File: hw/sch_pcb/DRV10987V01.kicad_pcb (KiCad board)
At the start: 2 copper layers, 50.3 x 40.1 mm, 28 parts, among them IC1 DRV10987DPWPR, J10 3v3 or 5v, J11 WAGO, J12 WAGO, J2 HEADER_2x05_PARALLEL, J3 HEADER_2x04_PARALLEL, J4 HEADER_2x01, J5 AUX, J6 HEADER_2x03_PARALLEL, M1 HOLE M3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

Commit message: update silkscreen, add 5v indicator
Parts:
- added D2: LED, Mlab_D:LED_1206_2, F.Cu at (127.9, 95.9)
- added R6: R_Small, Resistor_SMD:R_0805_2012Metric, F.Cu at (128.6, 98.5)
- J10: value 3v3 or 5v -> PWR
- J2: value HEADER_2x05_PARALLEL -> I2C
- J4: value HEADER_2x01 -> JUMPER
- J6: value HEADER_2x03_PARALLEL -> MOTOR
- L1: value 47uH -> 47uH DE0703-47
- M3, M4: value HOLE -> HOLE M3
- R1, R2, R3, R4, R5: value 4k5 -> 4k7
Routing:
- net +5V: track 34.1 -> 42.1 mm
- net Net-(D2-A): track 0.00 -> 2.71 mm
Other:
- board text added: "5V"
- board text added: "5V output 100 mA"
- board text added: "DRV10987V01A mlab.cz, 2023"
- board text removed: "2023"
- board text removed: "5V/3V3 output 100 mA configurable"
- board text removed: "DRV10975V01A mlab.cz"

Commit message: Zmena strany sroubu
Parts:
- M1, M2, M3, M4: moved to B.Cu
- turned M1 to 180 degrees
- turned M2 to 180 degrees
- turned M3 to 180 degrees
- turned M4 to 180 degrees
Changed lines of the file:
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@@
-    )
-  )
-  (footprint "Mlab_Mechanical:MountingHole_3mm" placed (layer "F.Cu")
-    (at 168.82 89.76)
-    (descr "Mounting hole, Befestigungsbohrung, 3mm, No Annular, Kein Restring,")
-    (tags "Mounting hole, Befestigungsbohrung, 3mm, No Annular, Kein Restring,")
-    (property "Sheetfile" "DRV10987V01.kicad_sch")
-    (property "Sheetname" "")
-    (attr through_hole)
-    (fp_text reference "M2" (at 0 -4.191) (layer "F.SilkS") hide
-        (effects (font (size 1.524 1.524) (thickness 0.3048)))
-    )
-    (fp_text value "HOLE M3" (at 0 4.191) (layer "F.SilkS") hide
-        (effects (font (size 1.524 1.524) (thickness 0.3048)))
-    )
-    (fp_circle (center 0 0) (end 2.99974 0)
-      (stroke (width 0.381) (type solid)) (fill none) (layer "F.Fab"))
-    (pad "1" thru_hole circle (at 0 0) (size 6 6) (drill 3) (layers "*.Cu" "*.Mask")
-      (net 1 "GND") (pintype "input") (clearance 1) (zone_connect 2))
-    (model "${MLAB}/src/3d/mechanical/m3_komplet.step"
-      (offset (xyz 0 0 0))
-      (scale (xyz 1 1 1))
-      (rotate (xyz 0 0 0))
     )
   )
@@
       (net 1 "GND") (pintype "passive"))
     (model "${KICAD6_3DMODEL_DIR}/Capacitor_SMD.3dshapes/C_0805_2012Metric.wrl"
-      (offset (xyz 0 0 0))
-      (scale (xyz 1 1 1))
-      (rotate (xyz 0 0 0))
-    )
-  )
-  (footprint "Mlab_Mechanical:MountingHole_3mm" placed (layer "F.Cu")
-    (at 168.82 120.24)
-    (descr "Mounting hole, Befestigungsbohrung, 3mm, No Annular, Kein Restring,")
-    (tags "Mounting hole, Befestigungsbohrung, 3mm, No Annular, Kein Restring,")
-    (property "Sheetfile" "DRV10987V01.kicad_sch")
-    (property "Sheetname" "")
-    (attr through_hole)
-    (fp_text reference "M4" (at 0 -4.191) (layer "F.SilkS") hide
-        (effects (font (size 1.524 1.524) (thickness 0.3048)))
-    )
-    (fp_text value "HOLE M3" (at 0 4.191) (layer "F.SilkS") hide
-        (effects (font (size 1.524 1.524) (thickness 0.3048)))
-    )
-    (fp_circle (center 0 0) (end 2.99974 0)
-      (stroke (width 0.381) (type solid)) (fill none) (layer "F.Fab"))
-    (pad "1" thru_hole circle (at 0 0) (size 6 6) (drill 3) (layers "*.Cu" "*.Mask")
-      (net 1 "GND") (pintype "input") (clearance 1) (zone_connect 2))
-    (model "${MLAB}/src/3d/mechanical/m3_komplet.step"
       (offset (xyz 0 0 0))
       (scale (xyz 1 1 1))
@@
       (net 6 "Net-(IC1-V3P3)") (pintype "passive"))
     (model "${KICAD6_3DMODEL_DIR}/Capacitor_SMD.3dshapes/C_0805_2012Metric.wrl"
-      (offset (xyz 0 0 0))
-      (scale (xyz 1 1 1))
-      (rotate (xyz 0 0 0))
-    )
-  )
-  (footprint "Mlab_Mechanical:MountingHole_3mm" placed (layer "F.Cu")
-    (at 128.18 120.24)
-    (descr "Mounting hole, Befestigungsbohrung, 3mm, No Annular, Kein Restring,")
-    (tags "Mounting hole, Befestigungsbohrung, 3mm, No Annular, Kein Restring,")
-    (property "Sheetfile" "DRV10987V01.kicad_sch")
-    (property "Sheetname" "")
-    (attr through_hole)
-    (fp_text reference "M3" (at 0 -4.191) (layer "F.SilkS") hide
-        (effects (font (size 1.524 1.524) (thickness 0.3048)))
-    )
-    (fp_text value "HOLE M3" (at 0 4.191) (layer "F.SilkS") hide
-        (effects (font (size 1.524 1.524) (thickness 0.3048)))
-    )
-    (fp_circle (center 0 0) (end 2.99974 0)
-      (stroke (width 0.381) (type solid)) (fill none) (layer "F.Fab"))
-    (pad "1" thru_hole circle (at 0 0) (size 6 6) (drill 3) (layers "*.Cu" "*.Mask")
-      (net 1 "GND") (pintype "input") (clearance 1) (zone_connect 2))
-    (model "${MLAB}/src/3d/mechanical/m3_komplet.step"
-      (offset (xyz 0 0 0))
-      (scale (xyz 1 1 1))
-      (rotate (xyz 0 0 0))
-    )
-  )
-  (footprint "Mlab_Mechanical:MountingHole_3mm" placed (layer "F.Cu")
-    (at 128.18 89.76)
-    (descr "Mounting hole, Befestigungsbohrung, 3mm, No Annular, Kein Restring,")
-    (tags "Mounting hole, Befestigungsbohrung, 3mm, No Annular, Kein Restring,")
-    (property "Sheetfile" "DRV10987V01.kicad_sch")
-    (property "Sheetname" "")
-    (attr through_hole)
-    (fp_text reference "M1" (at 0 -4.191) (layer "F.SilkS") hide
-        (effects (font (size 1.524 1.524) (thickness 0.3048)))
-    )
-    (fp_text value "HOLE M3" (at 0 4.191) (layer "F.SilkS") hide
-        (effects (font (size 1.524 1.524) (thickness 0.3048)))
-    )
-    (fp_circle (center 0 0) (end 2.99974 0)
-      (stroke (width 0.381) (type solid)) (fill none) (layer "F.Fab"))
-    (pad "1" thru_hole circle (at 0 0) (size 6 6) (drill 3) (layers "*.Cu" "*.Mask")
-      (net 1 "GND") (pintype "input") (clearance 1) (zone_connect 2))
-    (model "${MLAB}/src/3d/mechanical/m3_komplet.step"
       (offset (xyz 0 0 0))
       (scale (xyz 1 1 1))
@@
     )
   )
+  (footprint "Mlab_Mechanical:MountingHole_3mm" placed (layer "B.Cu")
+    (at 168.82 89.76 180)
+    (descr "Mounting hole, Befestigungsbohrung, 3mm, No Annular, Kein Restring,")
+    (tags "Mounting hole, Befestigungsbohrung, 3mm, No Annular, Kein Restring,")
+    (property "Sheetfile" "DRV10987V01.kicad_sch")
+    (property "Sheetname" "")
+    (attr through_hole)
+    (fp_text reference "M2" (at 0 4.191) (layer "B.SilkS") hide
+        (effects (font (size 1.524 1.524) (thickness 0.3048)) (justify mirror))
+    )
+    (fp_text value "HOLE M3" (at 0 -4.191) (layer "B.SilkS") hide
+        (effects (font (size 1.524 1.524) (thickness 0.3048)) (justify mirror))
+    )
+    (fp_circle (center 0 0) (end 2.99974 0)
+      (stroke (width 0.381) (type solid)) (fill none) (layer "B.Fab"))
+    (pad "1" thru_hole circle (at 0 0 180) (size 6 6) (drill 3) (layers "*.Cu" "*.Mask")
+      (net 1 "GND") (pintype "input") (clearance 1) (zone_connect 2))
+    (model "${MLAB}/src/3d/mechanical/m3_komplet.step"
+      (offset (xyz 0 0 0))
+      (scale (xyz 1 1 1))
+      (rotate (xyz 0 0 0))
+    )
+  )
   (footprint "TerminalBlock_WAGO:TerminalBlock_WAGO_236-102_1x02_P5.00mm_45Degree" (layer "B.Cu")
     (at 139.57 95.05)
@@
     (model "${KICAD6_3DMODEL_DIR}/Connector_PinHeader_2.54mm.3dshapes/PinHeader_1x02_P2.54mm_Vertical.wrl"
       (offset (xyz 0 1.27 0))
+      (scale (xyz 1 1 1))
+      (rotate (xyz 0 0 0))
+    )
+  )
+  (footprint "Mlab_Mechanical:MountingHole_3mm" placed (layer "B.Cu")
+    (at 168.82 120.24 180)
+    (descr "Mounting hole, Befestigungsbohrung, 3mm, No Annular, Kein Restring,")
+    (tags "Mounting hole, Befestigungsbohrung, 3mm, No Annular, Kein Restring,")
+    (property "Sheetfile" "DRV10987V01.kicad_sch")
+    (property "Sheetname" "")
+    (attr through_hole)
+    (fp_text reference "M4" (at 0 4.191) (layer "B.SilkS") hide
+        (effects (font (size 1.524 1.524) (thickness 0.3048)) (justify mirror))
+    )
+    (fp_text value "HOLE M3" (at 0 -4.191) (layer "B.SilkS") hide
+        (effects (font (size 1.524 1.524) (thickness 0.3048)) (justify mirror))
+    )
+    (fp_circle (center 0 0) (end 2.99974 0)
+      (stroke (width 0.381) (type solid)) (fill none) (layer "B.Fab"))
+    (pad "1" thru_hole circle (at 0 0 180) (size 6 6) (drill 3) (layers "*.Cu" "*.Mask")
+      (net 1 "GND") (pintype "input") (clearance 1) (zone_connect 2))
+    (model "${MLAB}/src/3d/mechanical/m3_komplet.step"
+      (offset (xyz 0 0 0))
       (scale (xyz 1 1 1))
       (rotate (xyz 0 0 0))
@@
     )
   )
+  (footprint "Mlab_Mechanical:MountingHole_3mm" placed (layer "B.Cu")
+    (at 128.18 120.24 180)
+    (descr "Mounting hole, Befestigungsbohrung, 3mm, No Annular, Kein Restring,")
+    (tags "Mounting hole, Befestigungsbohrung, 3mm, No Annular, Kein Restring,")
+    (property "Sheetfile" "DRV10987V01.kicad_sch")
+    (property "Sheetname" "")
+    (attr through_hole)
+    (fp_text reference "M3" (at 0 4.191) (layer "B.SilkS") hide
+        (effects (font (size 1.524 1.524) (thickness 0.3048)) (justify mirror))
+    )
+    (fp_text value "HOLE M3" (at 0 -4.191) (layer "B.SilkS") hide
+        (effects (font (size 1.524 1.524) (thickness 0.3048)) (justify mirror))
+    )
+    (fp_circle (center 0 0) (end 2.99974 0)
+      (stroke (width 0.381) (type solid)) (fill none) (layer "B.Fab"))
+    (pad "1" thru_hole circle (at 0 0 180) (size 6 6) (drill 3) (layers "*.Cu" "*.Mask")
+      (net 1 "GND") (pintype "input") (clearance 1) (zone_connect 2))
+    (model "${MLAB}/src/3d/mechanical/m3_komplet.step"
+      (offset (xyz 0 0 0))
+      (scale (xyz 1 1 1))
+      (rotate (xyz 0 0 0))
+    )
+  )
   (footprint "Mlab_Pin_Headers:Straight_2x05" (layer "B.Cu")
     (at 143.74 120.59375 90)
@@
       (scale (xyz 1 1 1))
       (rotate (xyz 0 0 0))
+    )
+  )
+  (footprint "Mlab_Mechanical:MountingHole_3mm" placed (layer "B.Cu")
+    (at 128.18 89.76 180)
+    (descr "Mounting hole, Befestigungsbohrung, 3mm, No Annular, Kein Restring,")
+    (tags "Mounting hole, Befestigungsbohrung, 3mm, No Annular, Kein Restring,")
+    (property "Sheetfile" "DRV10987V01.kicad_sch")
+    (property "Sheetname" "")
+    (attr through_hole)
+    (fp_text reference "M1" (at 0 4.191) (layer "B.SilkS") hide
+        (effects (font (size 1.524 1.524) (thickness 0.3048)) (justify mirror))
+    )
+    (fp_text value "HOLE M3" (at 0 -4.191) (layer "B.SilkS") hide
+        (effects (font (size 1.524 1.524) (thickness 0.3048)) (justify mirror))
+    )
+    (fp_circle (center 0 0) (end 2.99974 0)
+      (stroke (width 0.381) (type solid)) (fill none) (layer "B.Fab"))
+    (pad "1" thru_hole circle (at 0 0 180) (size 6 6) (drill 3) (layers "*.Cu" "*.Mask")
+      (net 1 "GND") (pintype "input") (clearance 1) (zone_connect 2))
+    (model "${MLAB}/src/3d/mechanical/m3_komplet.step"
+      (offset (xyz 0 0 0))
+      (scale (xyz 1 1 1))
+      (rotate (xyz 0 0 0))

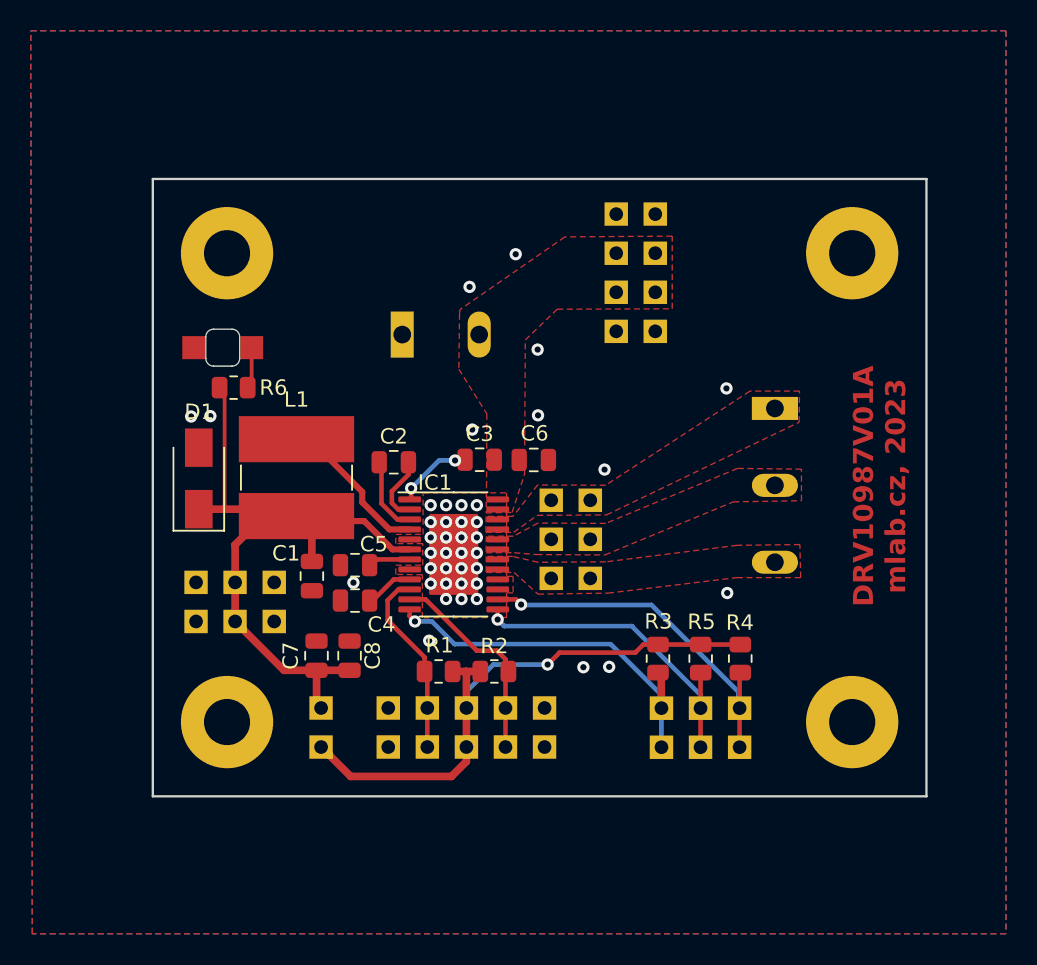
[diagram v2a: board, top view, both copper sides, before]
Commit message: uprava napajeni 3v3
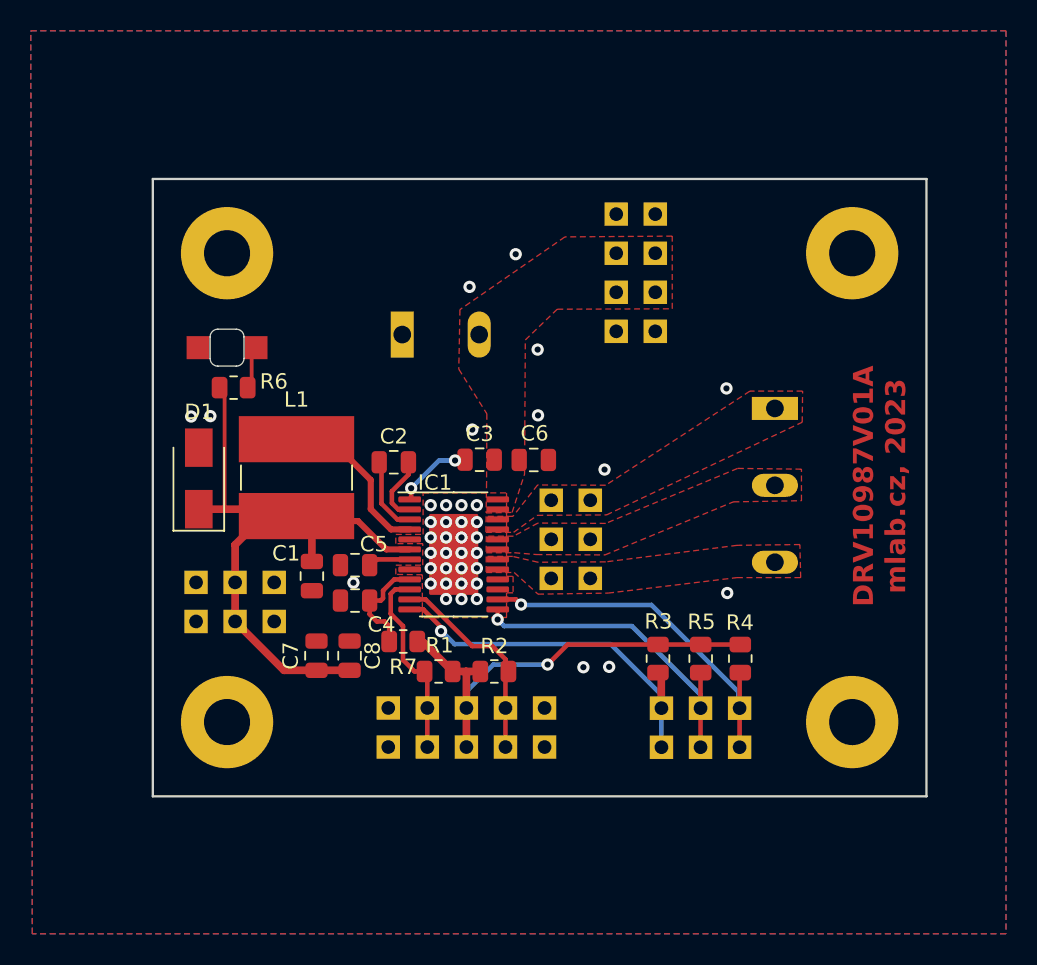
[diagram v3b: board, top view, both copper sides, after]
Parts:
- removed J4: JUMPER, Mlab_Pin_Headers:Straight_1x02
- added R7: 100R, Resistor_SMD:R_0805_2012Metric, F.Cu at (139.6, 115.0)
- R4, R5: value 4k7 -> DNF
- R6: value R_Small -> R
- moved D2 0.28 mm to (128.2, 95.9)
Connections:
- net Net-(IC1-V3P3) renamed /V3P3
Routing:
- net VDD: track 38.3 -> 29.8 mm
- net /V3P3: track 3.16 -> 6.93 mm
- net +5V: track 42.1 -> 39.6 mm
- net Net-(IC1-SW): track 10.1 -> 8.30 mm
- net GND: vias 41 -> 40

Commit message: repair silkscreen
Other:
- board text removed: "VCC-5V"
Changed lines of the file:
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@@
     (effects (font (size 1.3 1.3) (thickness 0.2) bold) (justify left bottom mirror))
-  )
-  (gr_text "VCC-5V" (at 131.645 122.925 270) (layer "B.SilkS")
-    (effects (font (size 1 0.8) (thickness 0.127)) (justify left bottom mirror))
   )
   (gr_text "GND  +12V  GND\n" (at 157.995 91.05 270) (layer "B.SilkS")

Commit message: Edit PCB and schema
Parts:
- C1, C3, C4, C5, C6, C7, C8, D2, IC1, L1, R1, R2, R3, R4, R5, R6, R7: moved to B.Cu
- C2: value 100nF -> 10nF; moved to B.Cu
- D1: footprint Diode_SMD:D_SMA -> Diode_SMD:D_MiniMELF; moved to B.Cu
- J10, J11, J12, J2, J3, J5, J6, M1, M2, M3, M4: moved to F.Cu
- moved M2 43.4 mm to (125.4, 89.8), turned to 0 degrees
- moved M4 43.4 mm to (125.4, 120.2), turned to 0 degrees
- moved D2 37.9 mm to (166.1, 95.9), turned to 0 degrees
- moved M1 37.9 mm to (166.1, 89.8), turned to 0 degrees
- moved M3 37.9 mm to (166.1, 120.2), turned to 0 degrees
- moved R6 37.0 mm to (165.6, 98.5), turned to 0 degrees
- moved J10 36.8 mm to (165.5, 112.4)
- moved D1 35.4 mm to (159.7, 116.4), turned to 180 degrees
- moved C7 34.6 mm to (167.8, 108.6), turned to 0 degrees
- moved J12 33.3 mm to (130.4, 99.8)
- moved C8 33.2 mm to (167.8, 105.8), turned to 0 degrees
- moved L1 28.8 mm to (161.5, 104.3)
- moved R4 28.8 mm to (132.7, 116.1)
- moved C1 26.8 mm to (160.5, 110.8)
- moved R5 23.7 mm to (135.3, 116.1)
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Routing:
- net +5V: track 39.6 -> 22.7 mm
- net /V3P3: track 6.93 -> 6.34 mm
- added copper zone on B.Cu, net +12V
- added copper zone on B.Cu, net +5V
- added copper zone on B.Cu, net /U
- added copper zone on B.Cu, net /V
- added copper zone on B.Cu, net /W
- removed copper zone on F.Cu, net +12V
- removed copper zone on F.Cu, net /U
- removed copper zone on F.Cu, net /V
- removed copper zone on F.Cu, net /W
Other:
- rule pad_to_mask_clearance: 0 -> 0.2
- board text added: "W V U"
- board text removed: "U V W"
